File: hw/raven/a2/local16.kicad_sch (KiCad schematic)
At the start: 32 parts, among them J105 IDE44, J402 Pinhdr_02x04, J403 BatteryHolder, U108 ATF22V10C-10PU, U304 MAX3245CAI+T, U406 DS1307, X101 8Mhz (5V), Y401 2.4576Mhz, Y402 32.768kHz

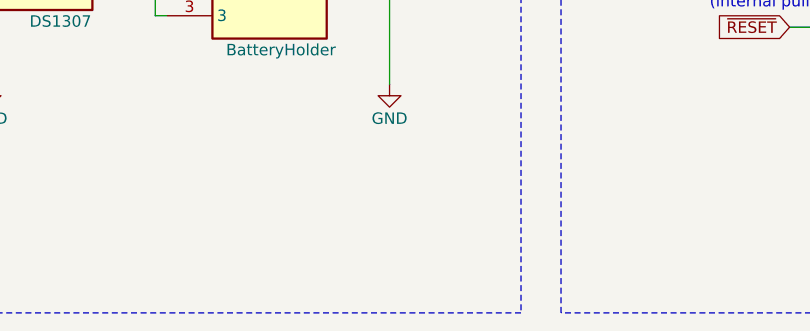
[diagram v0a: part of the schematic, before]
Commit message: rev.A2 updates
Added i2c DAC for reading cpu core temperature
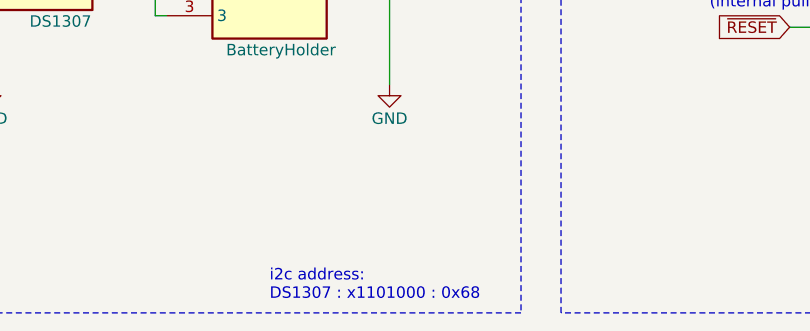
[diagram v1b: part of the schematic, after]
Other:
- note added: "i2c address: DS1307 : x1101000 : 0x68"
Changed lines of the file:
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@@
+    (effects (font (size 1.27 1.27)) (justify left bottom))
+  )
+  (text "i2c address:\nDS1307 : x1101000 : 0x68" (at 209.55 246.38 0)
     (effects (font (size 1.27 1.27)) (justify left bottom))
   )

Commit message: Raven.A2 wip
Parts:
- removed R402: 1K, Resistor_SMD:R_1206_3216Metric_Pad1.30x1.75mm_HandSolder, symbol Device:R
- added C414: 0.1u, Capacitor_SMD:C_1206_3216Metric_Pad1.33x1.80mm_HandSolder, symbol 68k:c_100nf_smd1206
- added R408: 2K2, Resistor_SMD:R_1206_3216Metric_Pad1.30x1.75mm_HandSolder, symbol Device:R
- added U407: 24AA02E48, Package_TO_SOT_SMD:SOT-23-5, symbol 68k:24AA02E48
- gave numbers to parts that had none: 7
- renumbered C514 to C403, C305 to C404, C305 to C405, C305 to C406, C305 to C407, C305 to C408, C306 to C409, C307 to C410, C308 to C411, C309 to C412, C305 to C413, J105 to J401, R109 to R403, R109 to R404, R109 to R406, R109 to R407, U108 to U402, U304 to U404, X101 to X401
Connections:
- net +5V: now also C414.2, U407.4 (VCC)
- net GND: now also C414.1, R408.2, U407.2 (VSS)
- net I2C_CLK: now also U407.1 (SCL); no longer J402.6 (Pin_6)
- net I2C_DTA: now also U407.3 (SDA); no longer J402.8 (Pin_8)
- net IDE:IRQ: now also R408.1
- net PD16: now also J401.17 (D0); no longer J401.4 (D8)
- net PD17: now also J401.15 (D1); no longer J401.6 (D9)
- net PD18: now also J401.13 (D2); no longer J401.8 (D10)
- net PD19: now also J401.11 (D3); no longer J401.10 (D11)
- net PD20: now also J401.9 (D4); no longer J401.12 (D12)
- net PD21: now also J401.7 (D5); no longer J401.14 (D13)
- net PD22: now also J401.5 (D6); no longer J401.16 (D14)
- net PD23: now also J401.3 (D7); no longer J401.18 (D15)
- net PD24: now also J401.4 (D8); no longer J401.17 (D0)
- net PD25: now also J401.6 (D9); no longer J401.15 (D1)
- net PD26: now also J401.8 (D10); no longer J401.13 (D2)
- net PD27: now also J401.10 (D11); no longer J401.11 (D3)
- net PD28: now also J401.12 (D12); no longer J401.9 (D4)
- net PD29: now also J401.14 (D13); no longer J401.7 (D5)
- net PD30: now also J401.16 (D14); no longer J401.5 (D6)
- net PD31: now also J401.18 (D15); no longer J401.3 (D7)
- no-connect marks 22 -> 25
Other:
- note added: "Big endian byte order as Atari"
- note added: "Pre-programmed MAC Address +128 byte eeprom"
- note added: "i2c address: 24AA02E48 : x1010010 : 0x52"
- note removed: "Little endian byte order"
- moved on the sheet: R406

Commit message: A2 fan pwm+argb
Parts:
- U407: Manufacturer_Part 24AA02E48T-I/OT -> (none); Manufacturer_Part_Number (none) -> 24AA02E48T-I/OT
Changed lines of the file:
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@@
 			)
 		)
-		(property "Manufacturer_Part" "24AA02E48T-I/OT"
+		(property "Manufacturer_Part_Number" "24AA02E48T-I/OT"
 			(at 165.1 274.32 0)
 			(effects

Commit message: a2 wip
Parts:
- renumbered R406 to R405, R408 to R406
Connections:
- net +5V: no longer C413.2, U406.8 (VCC)
- new net +5VL: C413.2, U406.8 (VCC)

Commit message: minor fixes
- replace IDE header footprint and part
- fix floating (unused) inputs on U102
- removed ckbd debug pads
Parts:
- J401: footprint 68k:SHDR44W55P200_2X22_4665X630X640P -> 68k:IDE44PIN; Manufacturer_Name Molex -> Wurth; Manufacturer_Part_Number 87831-4420 -> 62004421121
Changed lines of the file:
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@@
 			)
 		)
-		(property "Footprint" "68k:SHDR44W55P200_2X22_4665X630X640P"
+		(property "Footprint" "68k:IDE44PIN"
 			(at 58.42 194.945 0)
 			(effects
@@
 			)
 		)
-		(property "Description" ""
-			(at 90.17 191.135 0)
+		(property "Description" "Connector pin header"
+			(at 101.6 225.425 0)
 			(effects
 				(font
 					(size 1.27 1.27)
 				)
+				(hide yes)
 			)
 		)
-		(property "Manufacturer_Name" "Molex"
+		(property "Manufacturer_Name" "Wurth"
 			(at 90.17 191.135 0)
 			(effects
@@
 			)
 		)
-		(property "Manufacturer_Part_Number" "87831-4420"
+		(property "Manufacturer_Part_Number" "62004421121"
 			(at 90.17 191.135 0)
 			(effects

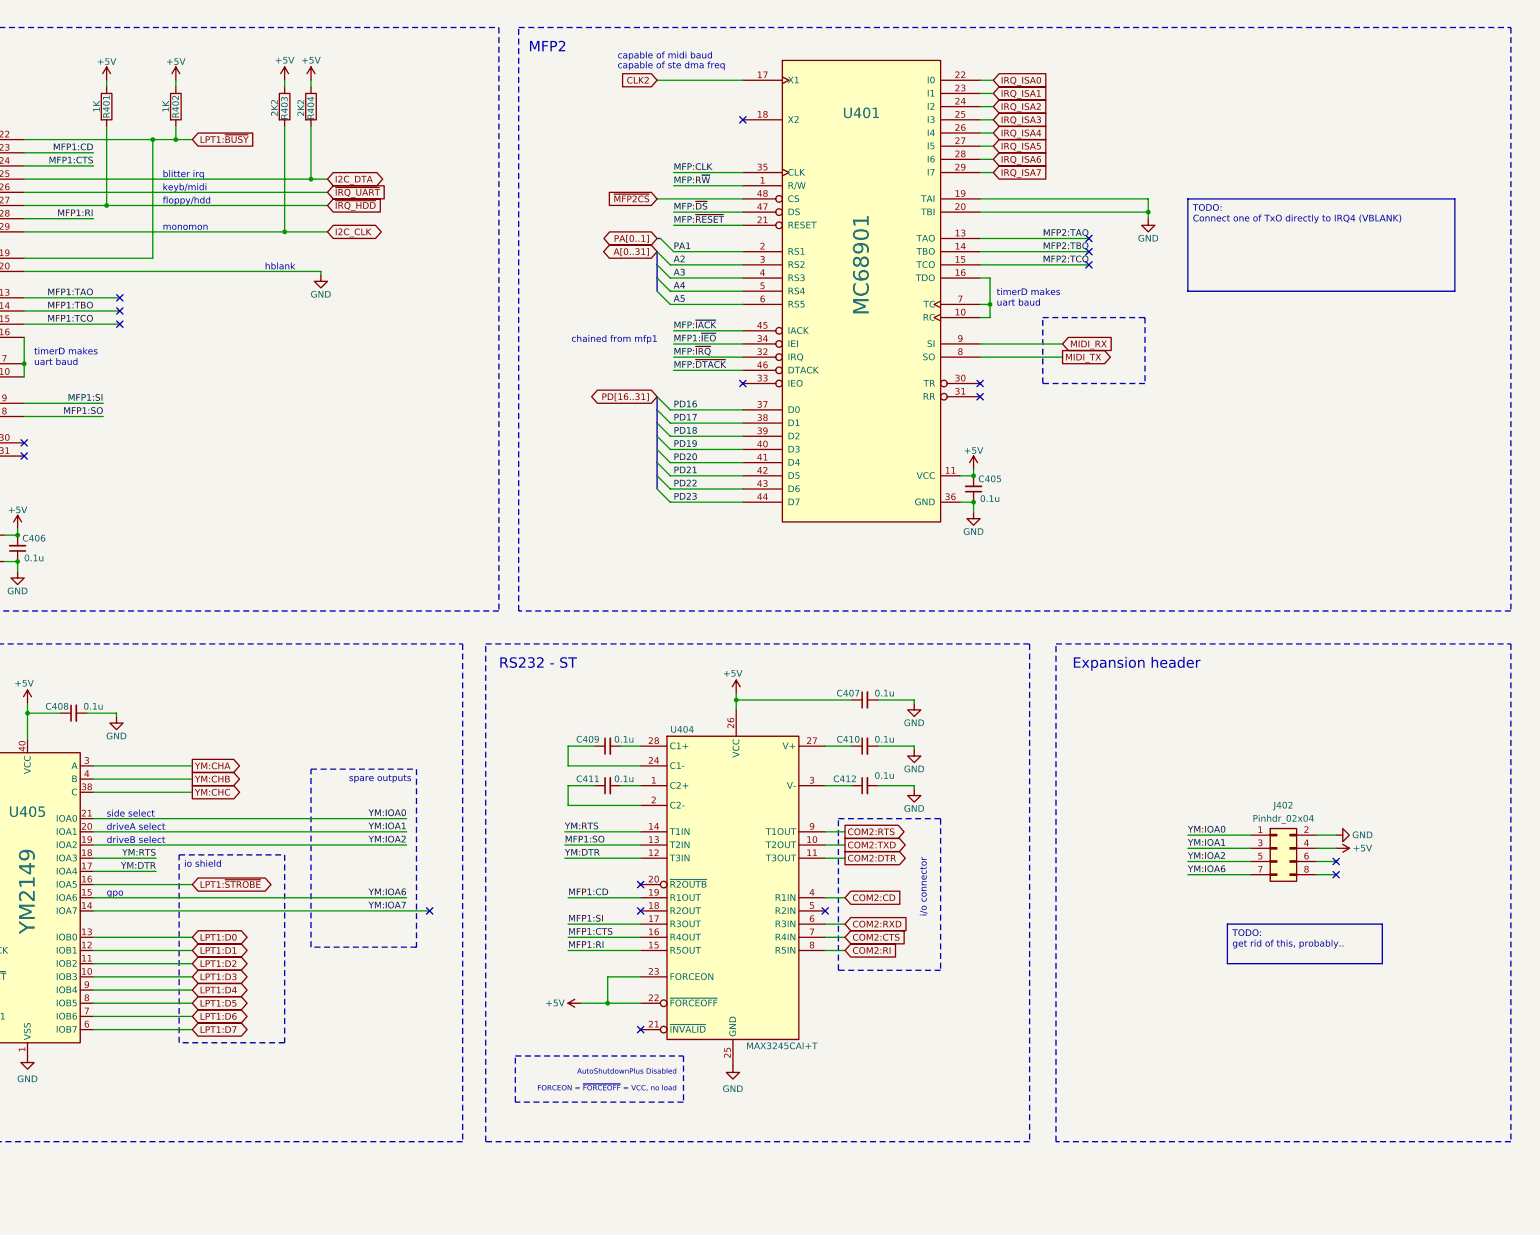
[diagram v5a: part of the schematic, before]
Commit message: A2 rework
- reworking top-left area for dsp56303
- internal speaker header for YM
- software controlled volume for YM
- misc routing cleanup
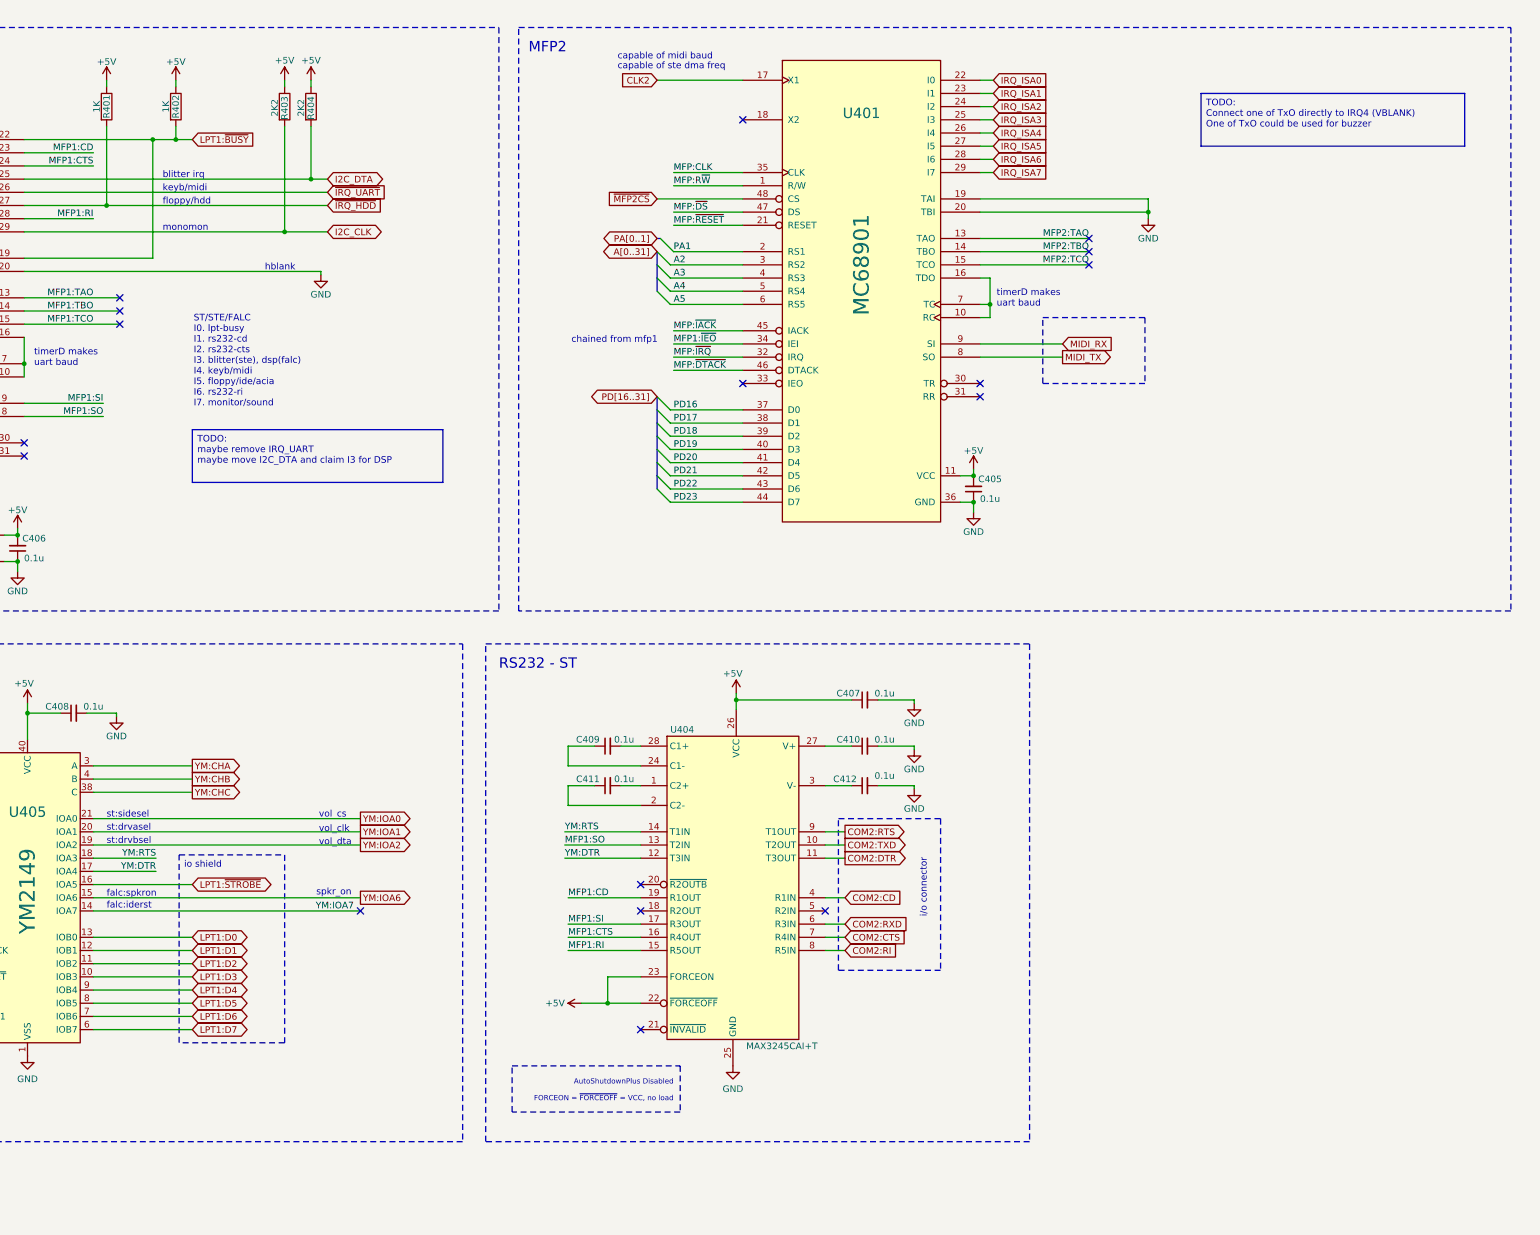
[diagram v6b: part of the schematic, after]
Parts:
- removed J402: Pinhdr_02x04, Connector_PinHeader_2.54mm:PinHeader_2x04_P2.54mm_Vertical, symbol Connector_Generic:Conn_02x04_Odd_Even
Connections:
- no-connect marks 25 -> 23
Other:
- note added: "ST/STE/FALC I0. lpt-busy I1. rs232-cd I2. rs232-cts I3. blitter(ste), dsp(falc) I4. keyb/midi I5. floppy/ide/acia I6. rs232-ri I7. monitor/sound"
- note added: "falc:iderst"
- note added: "falc:spkron"
- note added: "spkr_on"
- note added: "st:drvasel"
- note added: "st:drvbsel"
- note added: "st:sidesel"
- note added: "vol_clk"
- note added: "vol_cs"
- note added: "vol_dta"
- note removed: "Expansion header"
- note removed: "driveA select"
- note removed: "driveB select"
- note removed: "gpo"
- note removed: "side select"

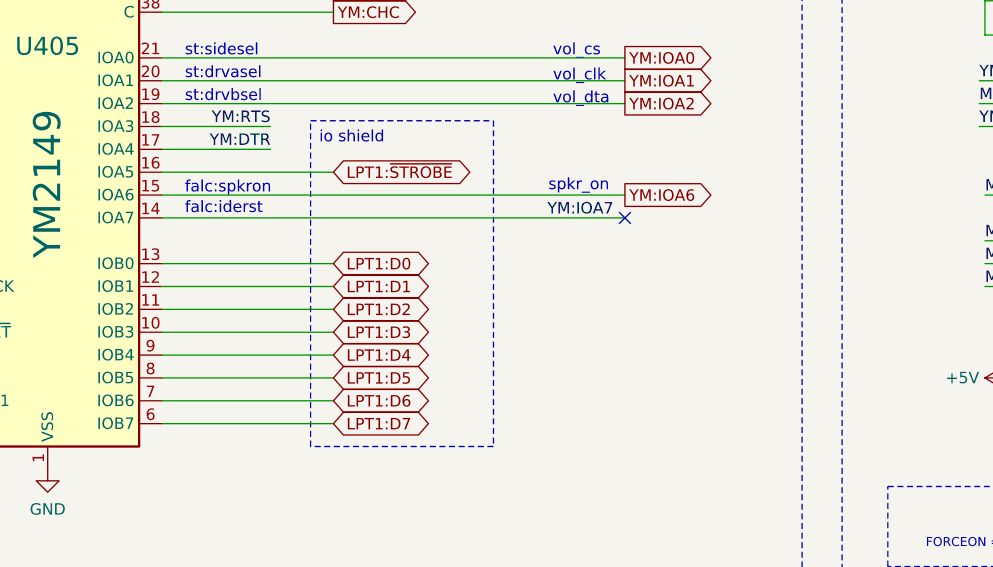
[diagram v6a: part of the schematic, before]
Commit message: A2. YM:IOA7 used for detecting volume+spkr controls
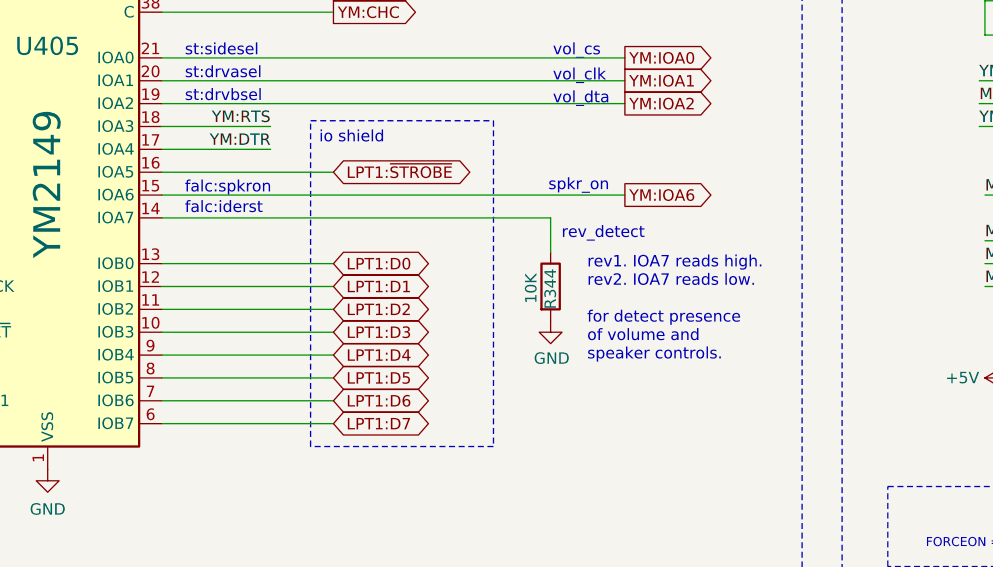
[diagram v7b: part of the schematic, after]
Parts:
- added R344: 10K, Resistor_SMD:R_1206_3216Metric_Pad1.30x1.75mm_HandSolder, symbol Device:R
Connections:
- net GND: now also R344.2
- net YM:IOA7: no longer names the net of U405.14 (IOA7)
- net YM:IOA7: now also R344.1
- no-connect marks 23 -> 22
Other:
- note added: "rev1. IOA7 reads high. rev2. IOA7 reads low. for detect presence of volume and speaker controls."
- note added: "rev_detect"
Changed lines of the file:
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@@
 		)
 	)
+	(text "rev1. IOA7 reads high.\nrev2. IOA7 reads low.\n\nfor detect presence\nof volume and\nspeaker controls."
+		(exclude_from_sim no)
+		(at 348.234 213.36 0)
+		(effects
+			(font
+				(size 1.27 1.27)
+			)
+			(justify left)
+		)
+	)
 	(text "st:drvbsel"
 		(exclude_from_sim no)
@@
 		)
 	)
+	(text "rev_detect"
+		(exclude_from_sim no)
+		(at 350.012 204.978 0)
+		(effects
+			(font
+				(size 1.27 1.27)
+			)
+		)
+	)
 	(text "capable of ste dma freq"
 		(exclude_from_sim no)
@@
 	)
 	(no_connect
-		(at 352.425 203.2)
-	)
-	(no_connect
 		(at 406.4 198.12)
 	)
@@
 	(wire
 		(pts
+			(xy 344.17 203.2) (xy 344.17 207.01)
+		)
+		(stroke
+			(width 0)
+			(type default)
+		)
+	)
+	(wire
+		(pts
 			(xy 412.75 99.06) (xy 426.085 99.06)
 		)
@@
 	(wire
 		(pts
-			(xy 300.99 203.2) (xy 352.425 203.2)
+			(xy 300.99 203.2) (xy 344.17 203.2)
 		)
 		(stroke
@@
 		)
 	)
-	(label "YM:IOA7"
-		(at 351.155 203.2 180)
-		(effects
-			(font
-				(size 1.27 1.27)
-			)
-			(justify right bottom)
-		)
-	)
 	(label "A4"
 		(at 412.75 83.82 0)
@@
 					(unit 1)
 				)
+			)
+		)
+	)
+	(symbol
+		(lib_id "Device:R")
+		(at 344.17 210.82 0)
+		(unit 1)
+		(exclude_from_sim no)
+		(in_bom yes)
+		(on_board yes)
+		(dnp no)
+		(property "Reference" "R344"
+			(at 344.17 213.36 90)
+			(effects
+				(font
+					(size 1.27 1.27)
+				)
+				(justify left)
+			)
+		)
+		(property "Value" "10K"
+			(at 342.011 212.725 90)
+			(effects
+				(font
+					(size 1.27 1.27)
+				)
+				(justify left)
+			)
+		)
+		(property "Footprint" "Resistor_SMD:R_1206_3216Metric_Pad1.30x1.75mm_HandSolder"
+			(at 342.392 210.82 90)
+			(effects
+				(font
+					(size 1.27 1.27)
+				)
+				(hide yes)
+			)
+		)
+		(property "Datasheet" "~"
+			(at 344.17 210.82 0)
+			(effects
+				(font
+					(size 1.27 1.27)
+				)
+				(hide yes)
+			)
+		)
+		(property "Description" ""
+			(at 344.17 210.82 0)
+			(effects
+				(font
+					(size 1.27 1.27)
+				)
+			)
+		)
+		(property "Manufacturer_Name" "Yageo"
+			(at 344.17 210.82 90)
+			(effects
+				(font
+					(size 1.27 1.27)
+				)
+				(hide yes)
+			)
+		)
+		(property "Manufacturer_Part_Number" "RT1206FRE0710KL"
+			(at 344.17 210.82 90)
+			(effects
+				(font
+					(size 1.27 1.27)
+				)
+				(hide yes)
+			)
+		)
+		(pin "1"
+		)
+		(pin "2"
+		)
+		(instances
+			(project "raven"
+				(path "/af55e73e-5814-45b4-ac5c-0bab62c0b1c7/dacbbff1-3783-4e73-aa71-dbe41700eceb"
+					(reference "R344")
+					(unit 1)
+				)
+			)
+		)
+	)
+	(symbol
+		(lib_id "power:GND")
+		(at 344.17 214.63 0)
+		(unit 1)
+		(exclude_from_sim no)
+		(in_bom yes)
+		(on_board yes)
+		(dnp no)
+		(property "Reference" "#PWR0638"
+			(at 344.17 220.98 0)
+			(effects
+				(font
+					(size 1.27 1.27)
+				)
+				(hide yes)
+			)
+		)
+		(property "Value" "GND"
+			(at 344.297 218.821 0)
+			(effects
+				(font
+					(size 1.27 1.27)
+				)
+			)
+		)
+		(property "Footprint" ""
+			(at 344.17 214.63 0)
+			(effects
+				(font
+					(size 1.27 1.27)
+				)
+				(hide yes)
+			)
+		)
+		(property "Datasheet" ""
+			(at 344.17 214.63 0)
+			(effects
+				(font
+					(size 1.27 1.27)
+				)
+				(hide yes)
+			)
+		)
+		(property "Description" ""
+			(at 344.17 214.63 0)
+			(effects
+				(font
+					(size 1.27 1.27)
+				)
+			)
+		)
+		(pin "1"
+		)
+		(instances
+			(project "raven"
+				(path "/af55e73e-5814-45b4-ac5c-0bab62c0b1c7/dacbbff1-3783-4e73-aa71-dbe41700eceb"
+					(reference "#PWR0638")
+					(unit 1)
+				)

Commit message: A2: DSP ram routing
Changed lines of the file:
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@@
 			(font
 				(size 2 2)
+				(thickness 0.4)
+				(bold yes)
 			)
 			(justify left bottom)
@@
 			(font
 				(size 2 2)
+				(thickness 0.4)
+				(bold yes)
 			)
 			(justify left bottom)
@@
 			(font
 				(size 2 2)
+				(thickness 0.4)
+				(bold yes)
 			)
 			(justify left bottom)
@@
 			(font
 				(size 2 2)
+				(thickness 0.4)
+				(bold yes)
 			)
 			(justify left bottom)
@@
 			(font
 				(size 2 2)
+				(thickness 0.4)
+				(bold yes)
 			)
 			(justify left bottom)
@@
 			(font
 				(size 2 2)
+				(thickness 0.4)
+				(bold yes)
 			)
 			(justify left bottom)
@@
 			(font
 				(size 2 2)
+				(thickness 0.4)
+				(bold yes)
 			)
 			(justify left bottom)
@@
 			(font
 				(size 2 2)
-			)
-			(justify left bottom)
+				(thickness 0.4)
+				(bold yes)
+			)
+			(justify left bottom)
